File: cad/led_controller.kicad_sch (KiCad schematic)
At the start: 23 parts, among them M1 50 ≤ rpm ≤ 2000, SW1 Toggle switch, SW5 SW_Push, SW6 SW_Push, SW7 Toggle switch

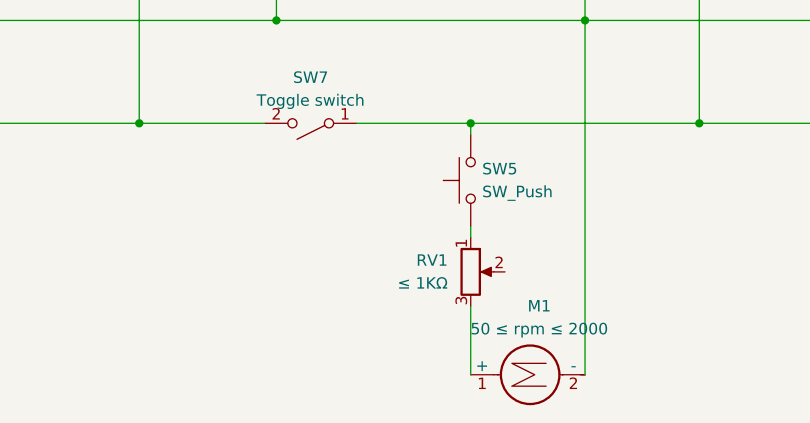
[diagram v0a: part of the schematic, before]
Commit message: make potentiometer maximum resistance accurate (10Kohm)
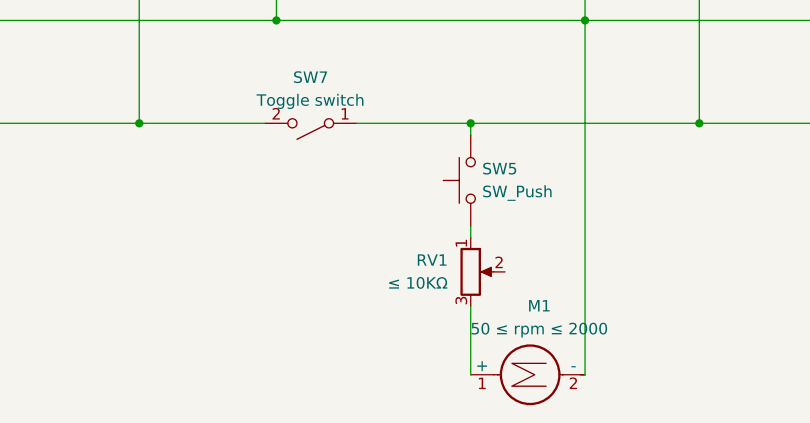
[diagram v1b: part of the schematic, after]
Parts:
- RV1: value ≤ 1KΩ -> ≤ 10KΩ
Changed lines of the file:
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@@
 			)
 		)
-		(property "Value" "≤ 1KΩ"
+		(property "Value" "≤ 10KΩ"
 			(at 176.53 137.1599 0)
 			(effects

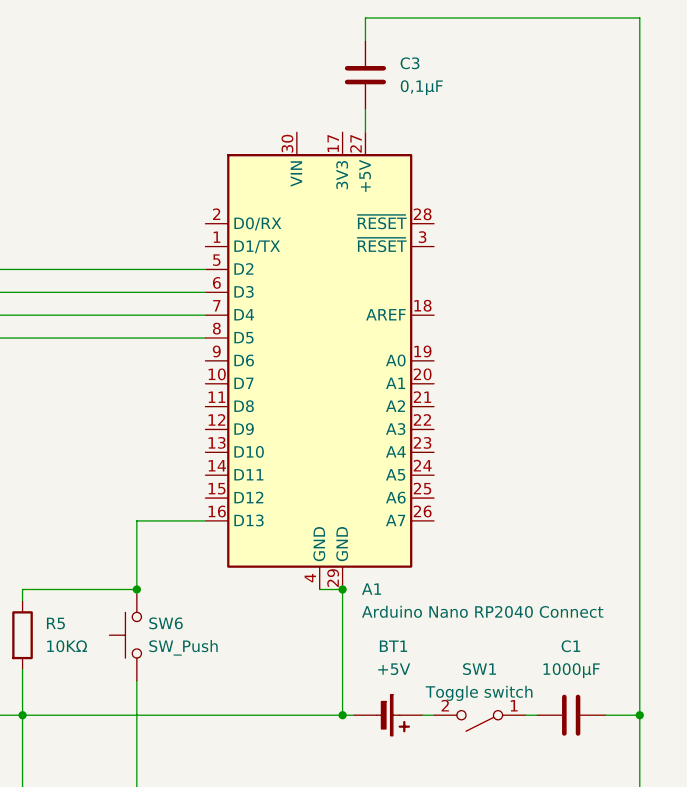
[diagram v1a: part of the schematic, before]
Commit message: change to more accurate board
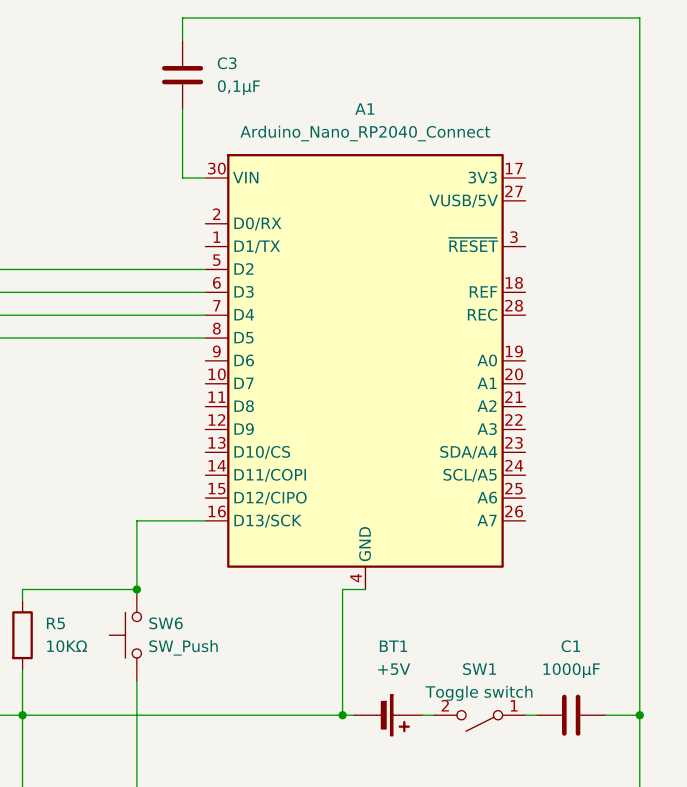
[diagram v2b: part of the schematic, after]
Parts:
- removed A1: Arduino Nano RP2040 Connect, Module:Arduino_Nano, symbol MCU_Module:Arduino_Nano_v2.x
- added A1: Arduino_Nano_RP2040_Connect, Module:Arduino_Nano, symbol MCU_Module:Arduino_Nano_RP2040_Connect
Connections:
- net at R4.1: now also A1.5 (D2)
- net at R5.1, SW6.2: now also A1.16 (D13/SCK)
- net at BT1.2 (-), D1.1 (VDD), D2.1 (VDD)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: now also A1.29 (GND), A1.4 (GND)
- net at C3.2: now also A1.30 (VIN)
- net at R3.1: now also A1.6 (D3)
- net at R2.1: now also A1.7 (D4)
- net at R1.1: now also A1.8 (D5)
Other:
- moved on the sheet: C3
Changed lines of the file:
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@@
-	)
-	(junction
-		(at 227.33 93.98)
-		(diameter 0)
-		(color 0 0 0 0)
 	)
 	(junction
@@
 	(wire
 		(pts
+			(xy 209.55 30.48) (xy 209.55 33.02)
+		)
+		(stroke
+			(width 0)
+			(type default)
+		)
+	)
+	(wire
+		(pts
 			(xy 260.35 119.38) (xy 260.35 107.95)
 		)
@@
 	(wire
 		(pts
+			(xy 209.55 40.64) (xy 209.55 48.26)
+		)
+		(stroke
+			(width 0)
+			(type default)
+		)
+	)
+	(wire
+		(pts
+			(xy 209.55 30.48) (xy 260.35 30.48)
+		)
+		(stroke
+			(width 0)
+			(type default)
+		)
+	)
+	(wire
+		(pts
 			(xy 212.09 86.36) (xy 204.47 86.36)
 		)
@@
 	(wire
 		(pts
-			(xy 224.79 93.98) (xy 227.33 93.98)
-		)
-		(stroke
-			(width 0)
-			(type default)
-		)
-	)
-	(wire
-		(pts
 			(xy 46.99 86.36) (xy 46.99 119.38)
 		)
@@
 	(wire
 		(pts
+			(xy 227.33 93.98) (xy 229.87 93.98)
+		)
+		(stroke
+			(width 0)
+			(type default)
+		)
+	)
+	(wire
+		(pts
 			(xy 54.61 49.53) (xy 54.61 41.91)
 		)
@@
 	(wire
 		(pts
-			(xy 229.87 40.64) (xy 229.87 43.18)
-		)
-		(stroke
-			(width 0)
-			(type default)
-		)
-	)
-	(wire
-		(pts
 			(xy 110.49 119.38) (xy 142.24 119.38)
 		)
@@
 	(wire
 		(pts
-			(xy 229.87 30.48) (xy 260.35 30.48)
-		)
-		(stroke
-			(width 0)
-			(type default)
-		)
-	)
-	(wire
-		(pts
 			(xy 86.36 44.45) (xy 182.88 44.45)
 		)
@@
 	(wire
 		(pts
-			(xy 229.87 30.48) (xy 229.87 33.02)
-		)
-		(stroke
-			(width 0)
-			(type default)
-		)
-	)
-	(wire
-		(pts
 			(xy 125.73 68.58) (xy 125.73 107.95)
 		)
@@
 		(pts
 			(xy 185.42 41.91) (xy 185.42 58.42)
+		)
+		(stroke
+			(width 0)
+			(type default)
+		)
+	)
+	(wire
+		(pts
+			(xy 209.55 48.26) (xy 212.09 48.26)
 		)
 		(stroke
@@
 	)
 	(symbol
-		(lib_id "MCU_Module:Arduino_Nano_v2.x")
-		(at 224.79 68.58 0)
-		(unit 1)
-		(exclude_from_sim no)
-		(in_bom yes)
-		(on_board yes)
-		(dnp no)
-		(fields_autoplaced yes)
-		(property "Reference" "A1"
-			(at 229.4733 93.98 0)
-			(effects
-				(font
-					(size 1.27 1.27)
-				)
-				(justify left)
-			)
-		)
-		(property "Value" "Arduino Nano RP2040 Connect"
-			(at 229.4733 96.52 0)
-			(effects
-				(font
-					(size 1.27 1.27)
-				)
-				(justify left)
-			)
-		)
-		(property "Footprint" "Module:Arduino_Nano"
-			(at 224.79 68.58 0)
-			(effects
-				(font
-					(size 1.27 1.27)
-					(italic yes)
-				)
-				(hide yes)
-			)
-		)
-		(property "Datasheet" "https://www.arduino.cc/en/uploads/Main/ArduinoNanoManual23.pdf"
-			(at 224.79 68.58 0)
-			(effects
-				(font
-					(size 1.27 1.27)
-				)
-				(hide yes)
-			)
-		)
-		(property "Description" "Arduino Nano v2.x"
-			(at 224.79 68.58 0)
-			(effects
-				(font
-					(size 1.27 1.27)
-				)
-				(hide yes)
-			)
-		)
-		(pin "13"
-		)
-		(pin "9"
-		)
-		(pin "8"
-		)
-		(pin "5"
-		)
-		(pin "6"
-		)
-		(pin "12"
-		)
-		(pin "7"
-		)
-		(pin "10"
-		)
-		(pin "23"
-		)
-		(pin "18"
-		)
-		(pin "15"
-		)
-		(pin "2"
-		)
-		(pin "1"
-		)
-		(pin "11"
-		)
-		(pin "30"
-		)
-		(pin "4"
-		)
-		(pin "3"
-		)
-		(pin "21"
-		)
-		(pin "16"
-		)
-		(pin "28"
-		)
-		(pin "14"
-		)
-		(pin "29"
-		)
-		(pin "27"
-		)
-		(pin "19"
-		)
-		(pin "20"
-		)
-		(pin "17"
-		)
-		(pin "22"
-		)
-		(pin "24"
-		)
-		(pin "25"
-		)
-		(pin "26"
-		)
-		(instances
-			(project ""
-				(path "/33db064c-d5ae-416f-86c1-c095f962d498"
-					(reference "A1")
-					(unit 1)
-				)
-			)
-		)
-	)
-	(symbol
 		(lib_id "Device:R")
 		(at 86.36 53.34 0)
@@
 				(path "/33db064c-d5ae-416f-86c1-c095f962d498"
 					(reference "R3")
+					(unit 1)
+				)
+			)
+		)
+	)
+	(symbol
+		(lib_id "MCU_Module:Arduino_Nano_RP2040_Connect")
+		(at 229.87 68.58 0)
+		(unit 1)
+		(exclude_from_sim no)
+		(in_bom yes)
+		(on_board yes)
+		(dnp no)
+		(fields_autoplaced yes)
+		(property "Reference" "A1"
+			(at 229.87 40.64 0)
+			(effects
+				(font
+					(size 1.27 1.27)
+				)
+			)
+		)
+		(property "Value" "Arduino_Nano_RP2040_Connect"
+			(at 229.87 43.18 0)
+			(effects
+				(font
+					(size 1.27 1.27)
+				)
+			)
+		)
+		(property "Footprint" "Module:Arduino_Nano"
+			(at 243.586 102.616 0)
+			(effects
+				(font
+					(size 1.27 1.27)
+					(italic yes)
+				)
+				(hide yes)
+			)
+		)
+		(property "Datasheet" "https://docs.arduino.cc/resources/datasheets/ABX00053-datasheet.pdf"
+			(at 268.986 100.076 0)
+			(effects
+				(font
+					(size 1.27 1.27)
+				)
+				(hide yes)
+			)
+		)
+		(property "Description" "Arduino Nano board based on the RP2040 microcontroller with a dual-core 133 MHz ARM Cortex-M0+ processor, 264 kB SRAM, and up to 16 MB flash memory. Operates at 3.3V, with 5V Micro USB input and 4-20V VIN. Features Wi-Fi®, Bluetooth® LE, digital and analog pins, and supports SPI, I2C, UART, and PIO. Includes a 6-axis IMU, RGB LED, microphone, and cryptographic chip for secure communication."
+			(at 438.912 97.536 0)
+			(effects
+				(font
+					(size 1.27 1.27)
+				)
+				(hide yes)
+			)
+		)
+		(pin "13"
+		)
+		(pin "30"
+		)
+		(pin "1"
+		)
+		(pin "6"
+		)
+		(pin "8"
+		)
+		(pin "9"
+		)
+		(pin "10"
+		)
+		(pin "11"
+		)
+		(pin "5"
+		)
+		(pin "12"
+		)
+		(pin "2"
+		)
+		(pin "7"
+		)
+		(pin "21"
+		)
+		(pin "29"
+		)
+		(pin "15"
+		)
+		(pin "18"
+		)
+		(pin "24"
+		)
+		(pin "27"
+		)
+		(pin "16"
+		)
+		(pin "4"
+		)
+		(pin "14"
+		)
+		(pin "17"
+		)
+		(pin "28"
+		)
+		(pin "20"
+		)
+		(pin "22"
+		)
+		(pin "23"
+		)
+		(pin "25"
+		)
+		(pin "26"
+		)
+		(pin "3"
+		)
+		(pin "19"
+		)
+		(instances
+			(project ""
+				(path "/33db064c-d5ae-416f-86c1-c095f962d498"
+					(reference "A1")
 					(unit 1)
 				)
@@
 	(symbol
 		(lib_id "Device:C")
-		(at 229.87 36.83 0)
+		(at 209.55 36.83 0)
 		(unit 1)
 		(exclude_from_sim no)
@@
 		(fields_autoplaced yes)
 		(property "Reference" "C3"
-			(at 233.68 35.5599 0)
+			(at 213.36 35.5599 0)
 			(effects
 				(font
@@
 		)
 		(property "Value" "0,1µF"
-			(at 233.68 38.0999 0)
+			(at 213.36 38.0999 0)
 			(effects
 				(font
@@
 		)
 		(property "Footprint" ""
-			(at 230.8352 40.64 0)
+			(at 210.5152 40.64 0)
 			(effects
 				(font
@@
 		)
 		(property "Datasheet" "~"
-			(at 229.87 36.83 0)
+			(at 209.55 36.83 0)
 			(effects
 				(font
@@
 		)
 		(property "Description" "Unpolarized capacitor"
-			(at 229.87 36.83 0)
-			(effects
-				(font
+			(at 209.55 36.83 0)
+			(effects
+				(font

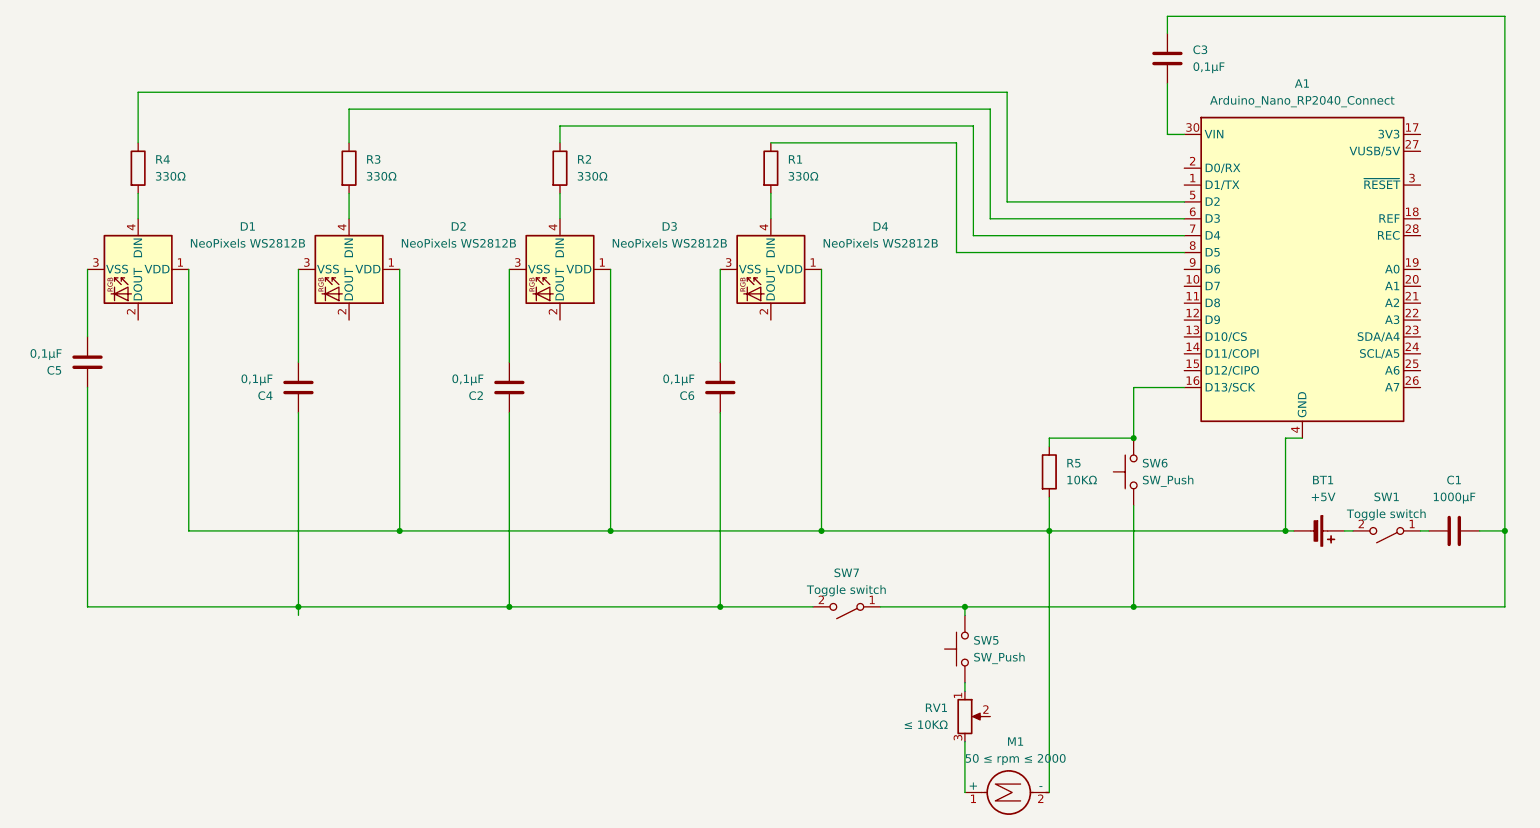
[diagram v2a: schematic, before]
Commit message: make capacitors parallel
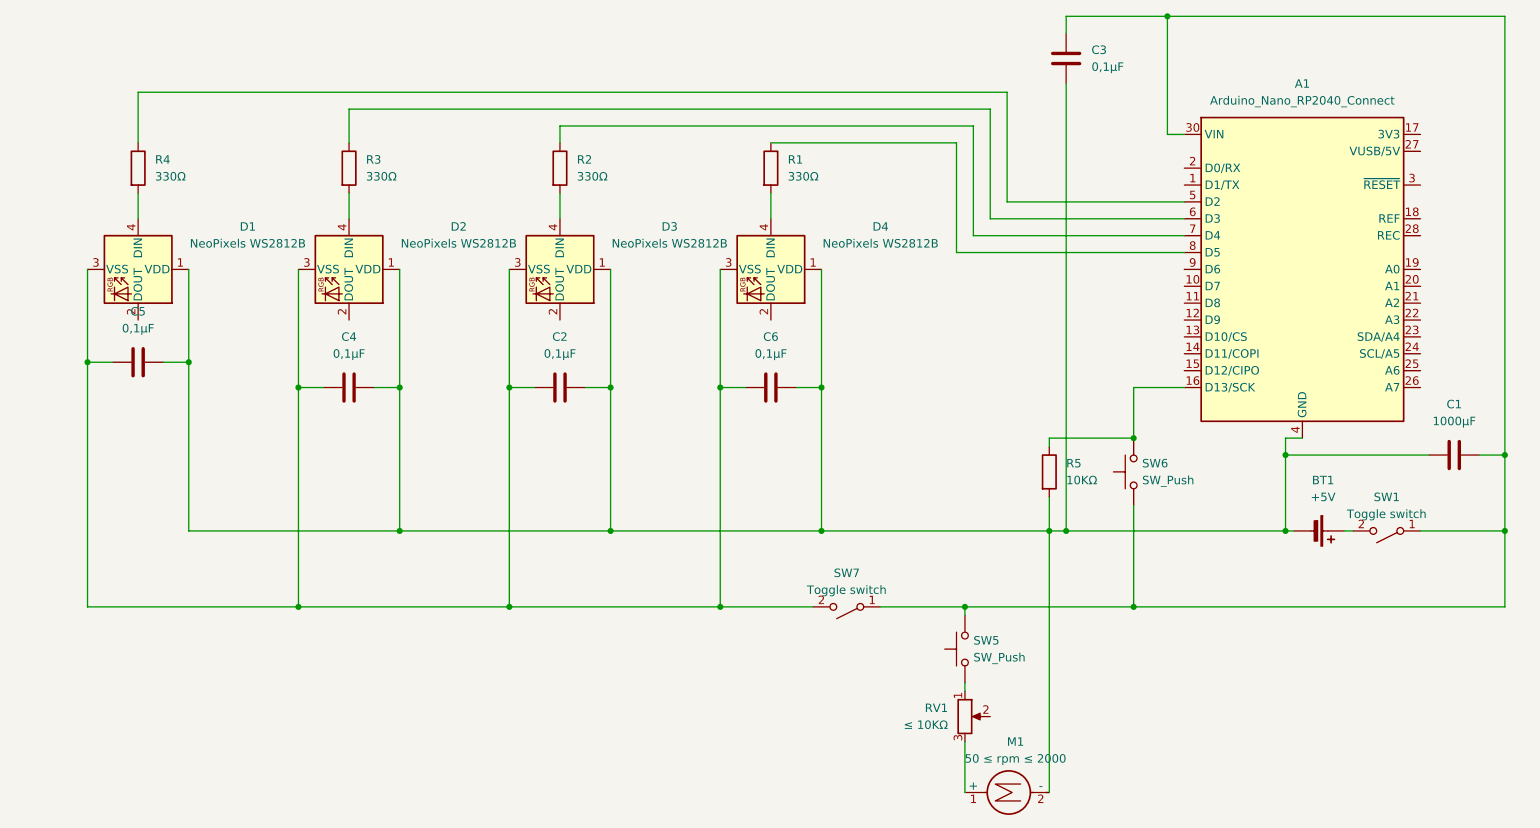
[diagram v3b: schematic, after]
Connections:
- net at C2.1, C4.1, C5.1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: now also A1.29 (GND), A1.4 (GND), BT1.2 (-), C1.2, C3.2, D1.1 (VDD), D2.1 (VDD), D3.1 (VDD), D4.1 (VDD), M1.2 (-), R5.2; no longer SW7.2 (B)
- net at C5.2, D1.3 (VSS): now also C2.2, C4.2, C6.2, D2.3 (VSS), D3.3 (VSS), D4.3 (VSS), SW7.2 (B)
- net at C1.1, C3.1, SW5.2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: now also A1.30 (VIN), SW1.1 (A)
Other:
- moved on the sheet: C1, C2, C3, C4, C5, C6

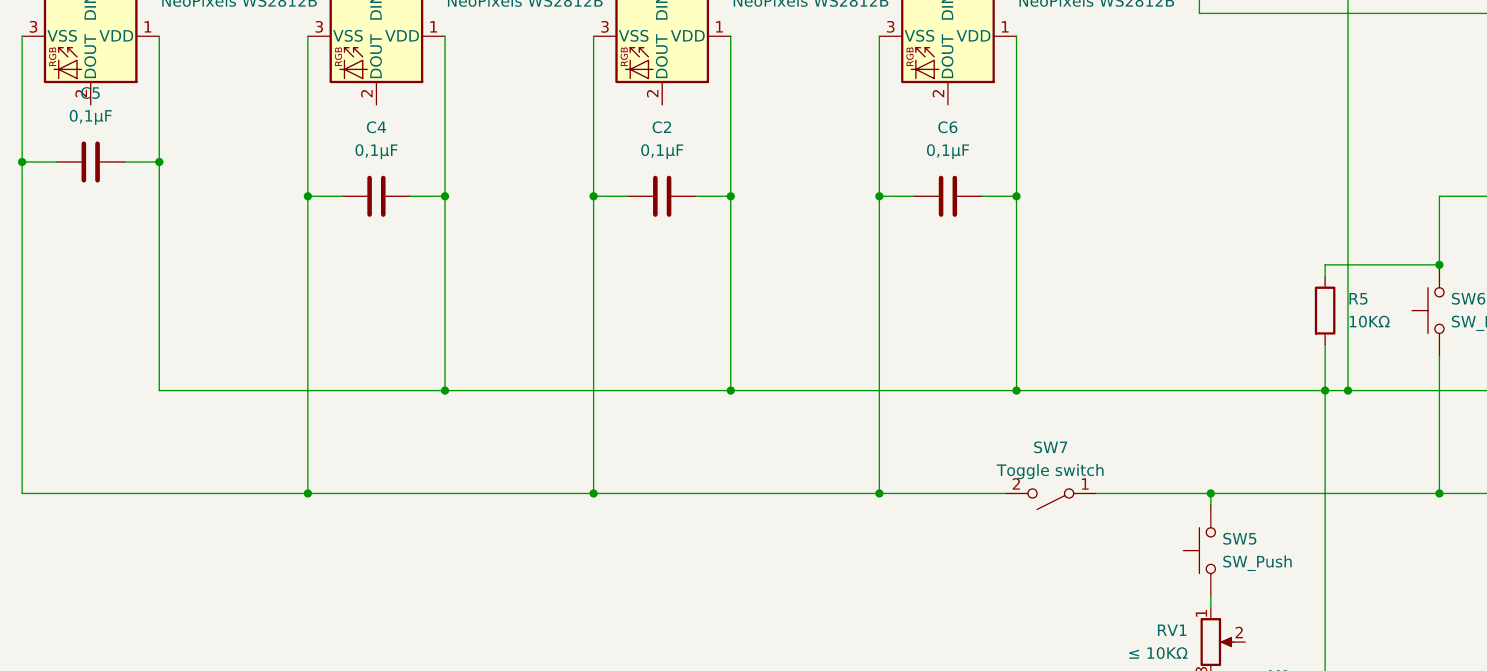
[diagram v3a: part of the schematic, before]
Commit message: Fixed VDD and VSS being connected in reverse
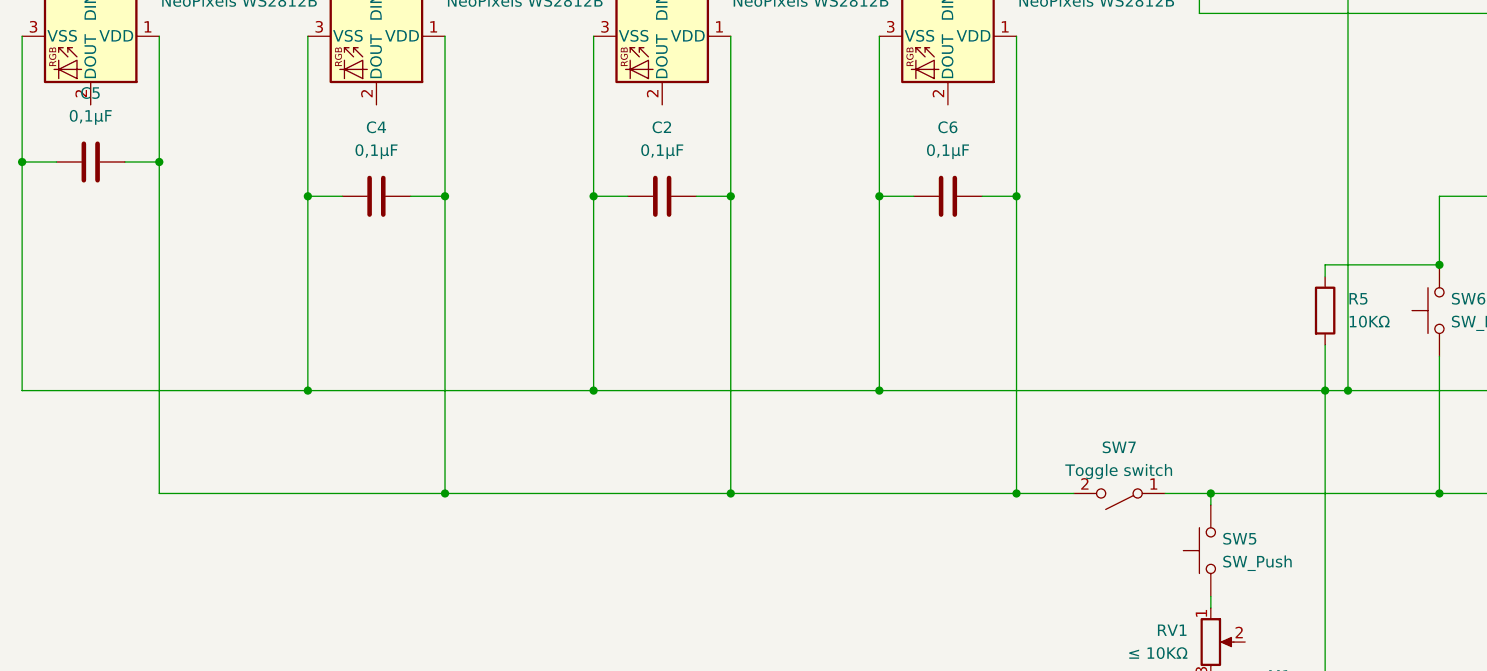
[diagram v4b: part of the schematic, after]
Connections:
- net at C2.1, C4.1, C5.1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: now also SW7.2 (B); no longer A1.29 (GND), A1.4 (GND), BT1.2 (-), C1.2, C3.2, M1.2 (-), R5.2
- net at C2.2, C4.2, C5.2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: now also A1.29 (GND), A1.4 (GND), BT1.2 (-), C1.2, C3.2, M1.2 (-), R5.2; no longer SW7.2 (B)
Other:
- moved on the sheet: SW7
